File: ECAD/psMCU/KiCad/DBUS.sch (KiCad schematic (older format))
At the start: 13 parts, among them U31 SN74LVC1G32DCK, U32 SN74LVC1G04DCK, U51 SN74HC245PW

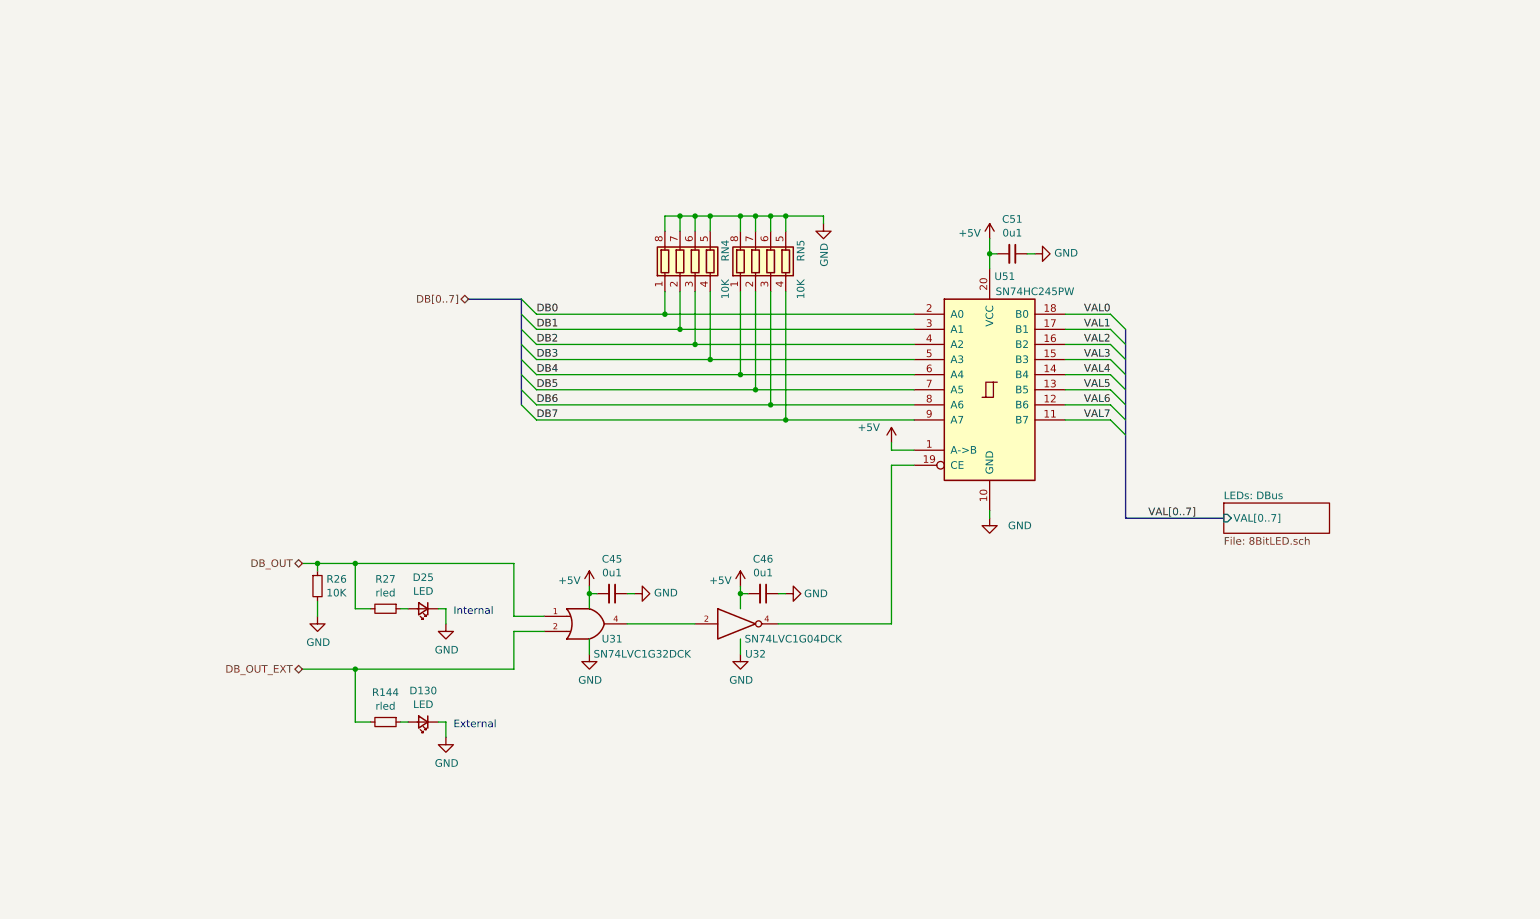
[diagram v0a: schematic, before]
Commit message: Sch: Implemented much improved debugger interface
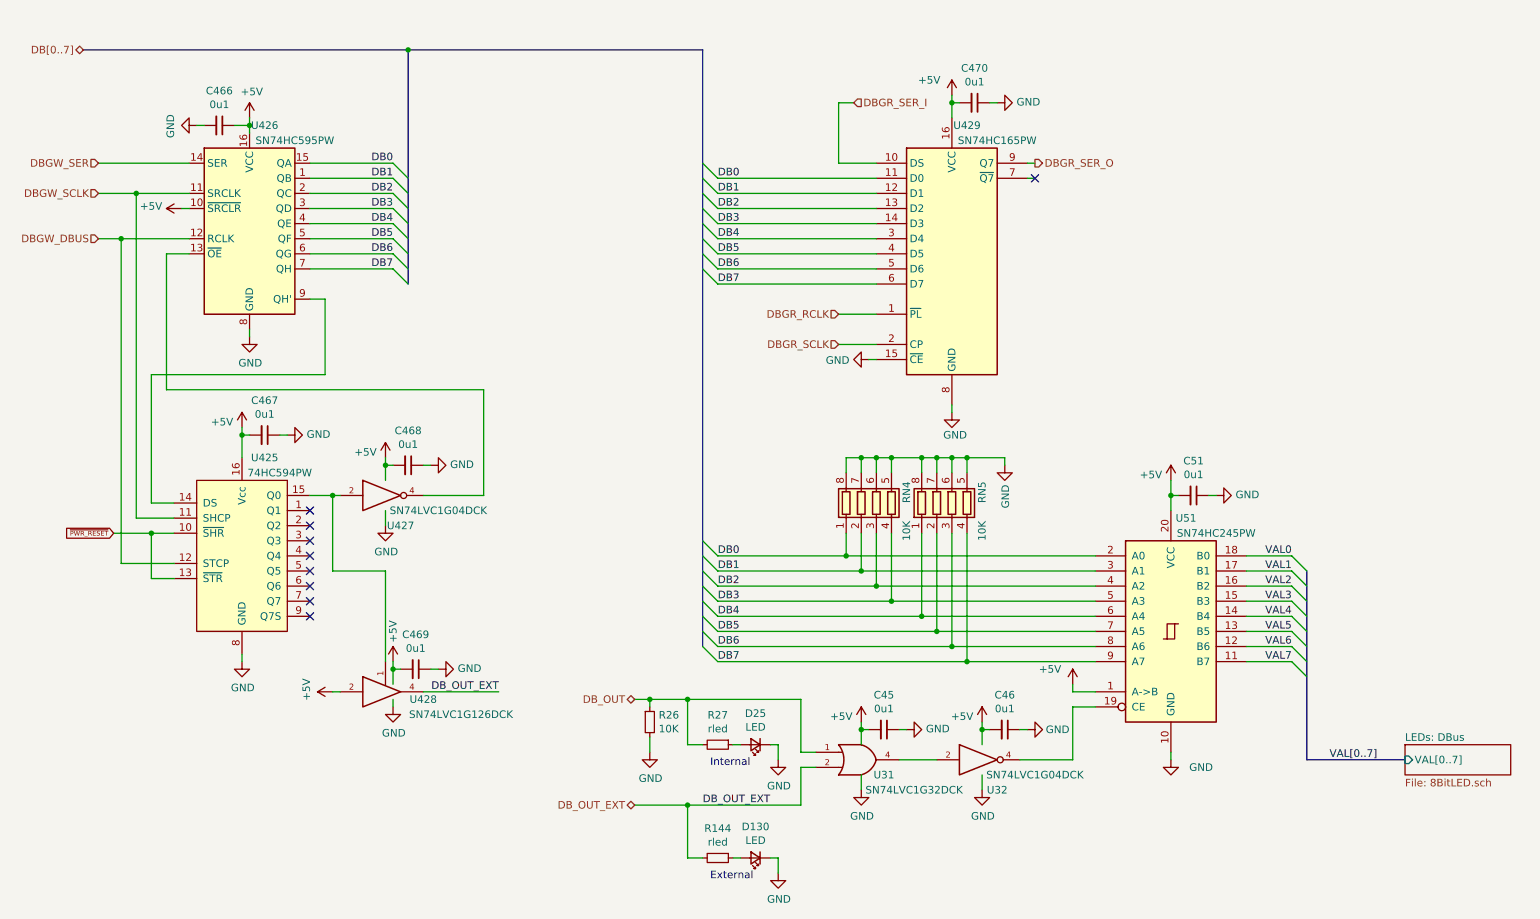
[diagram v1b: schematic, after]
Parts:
- added C466, C467, C468, C469, C470: 0u1, NoRef_Footprints:C_0603_1608Metric_NoRef, symbol Device:C_Small
- added U425: 74HC594PW, Package_SO:TSSOP-16_4.4x5mm_P0.65mm, symbol 74HC594:75HC594
- added U426: SN74HC595PW, Package_SO:TSSOP-16_4.4x5mm_P0.65mm, symbol 74xx:74HC595
- added U427: SN74LVC1G04DCK, Package_TO_SOT_SMD:SOT-353_SC-70-5, symbol 74xGxx:74LVC1G04
- added U428: SN74LVC1G126DCK, Package_TO_SOT_SMD:SOT-353_SC-70-5, symbol 74xGxx:74LVC1G126
- added U429: SN74HC165PW, Package_SO:TSSOP-16_4.4x5mm_P0.65mm, symbol 74xx:74LS165
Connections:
- net +5V: now also C466.1, C467.2, C468.2, C469.2, C470.2, U425.16 (Vcc), U426.10 (~SRCLR), U426.16 (VCC), U427.5 (VCC), U428.2, U428.5 (VCC), U429.16 (VCC)
- net DB0: now also U426.15 (QA), U429.11 (D0)
- net DB1: now also U426.1 (QB), U429.12 (D1)
- net DB2: now also U426.2 (QC), U429.13 (D2)
- net DB3: now also U426.3 (QD), U429.14 (D3)
- net DB4: now also U426.4 (QE), U429.3 (D4)
- net DB5: now also U426.5 (QF), U429.4 (D5)
- net DB6: now also U426.6 (QG), U429.5 (D6)
- net DB7: now also U426.7 (QH), U429.6 (D7)
- net DB_OUT_EXT: now also U428.4
- net GND: now also C466.2, C467.1, C468.1, C469.1, C470.1, U425.8 (GND), U426.8 (GND), U427.3 (GND), U428.3 (GND), U429.15 (~CE), U429.8 (GND)
- new net: U426.13 (~OE), U427.4
- new net: U425.14 (DS), U426.9 (QH')
- new net: U425.15 (Q0), U427.2, U428.1
- new net DBGR_RCLK: U429.1 (~PL)
- new net DBGR_SCLK: U429.2 (CP)
- new net DBGR_SER_I: U429.10 (DS)
- new net DBGR_SER_O: U429.9 (Q7)
- new net DBGW_DBUS: U425.12 (STCP), U426.12 (RCLK)
- new net DBGW_SCLK: U425.11 (SHCP), U426.11 (SRCLK)
- new net DBGW_SER: U426.14 (SER)
- new net ~PWR_RESET: U425.10 (~SHR), U425.13 (~STR)
- no-connect marks 0 -> 9
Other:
- moved on the sheet: C45, C46, C51, D130, D25, R144, R26, R27, RN4, RN5, U31, U32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

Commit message: Sch: Cleanup + Small fixes
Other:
- note added: "Bus Display"
- note added: "Debugger Input"
- note added: "Debugger Output"
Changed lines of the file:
@@
 $Descr A4 11693 8268
 encoding utf-8
-Sheet 101 109
+Sheet 2 109
 Title "psMCU"
 Date "2022-02-13"
@@
 Entry Wire Line
 	5450 5150 5350 5050
-Text HLabel 1250 1100 0    50   3State ~ 0
+Text HLabel 1250 900  0    50   3State ~ 0
 DB[0..7]
 Text Label 5450 5150 0    50   ~ 0
@@
 	2900 4050 2950 4050
 Wire Bus Line
-	3400 1100 1250 1100
+	3400 900  1250 900
 Wire Bus Line
-	3400 1100 5350 1100
-Connection ~ 3400 1100
+	3400 900  5350 900
+Connection ~ 3400 900
 Text Label 5350 6100 0    50   ~ 0
 DB_OUT_EXT
@@
 Wire Wire Line
 	3500 5350 4000 5350
+Text Notes 1800 1200 0    100  ~ 0
+Debugger Output
+Text Notes 6450 1100 0    100  ~ 0
+Debugger Input
+Text Notes 8000 3600 0    100  ~ 0
+Bus Display
 Wire Bus Line
-	3400 1100 3400 2650
+	3400 900  3400 2650
 Wire Bus Line
 	9350 4550 9350 5800
 Wire Bus Line
-	5350 1100 5350 5050
+	5350 900  5350 5050
 $EndSCHEMATC
